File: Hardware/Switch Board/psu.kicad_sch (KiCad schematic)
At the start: 3 parts, among them J1 691218410003

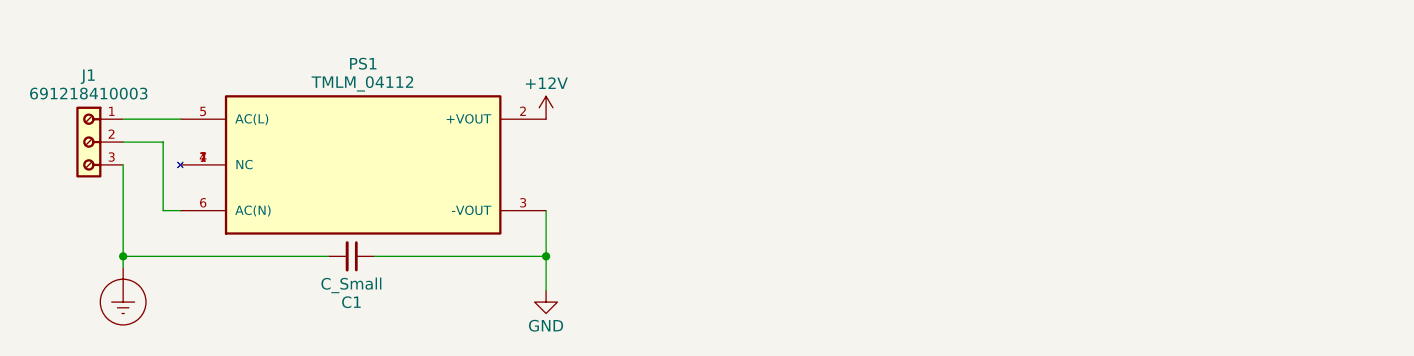
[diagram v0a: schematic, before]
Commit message: Completed Power Supply scheamatic + started to place components
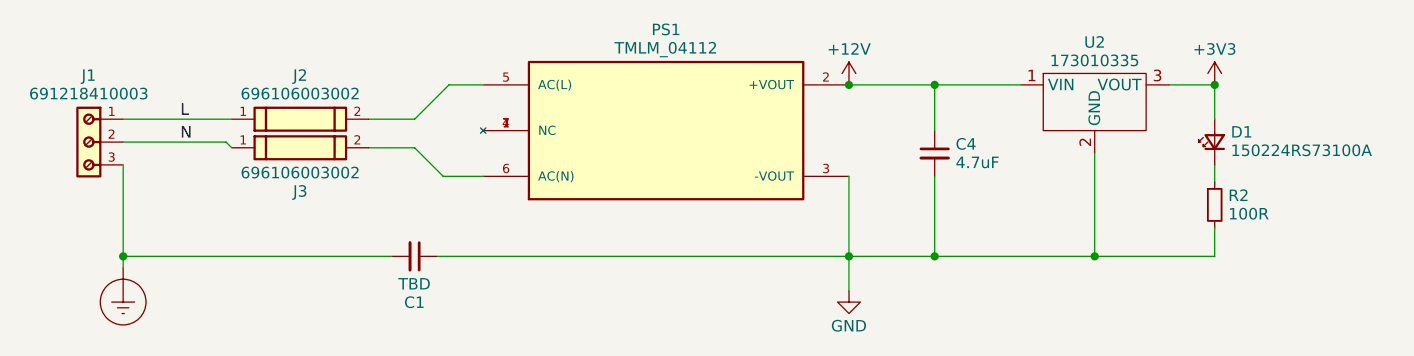
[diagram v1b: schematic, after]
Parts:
- added C4: 4.7uF, Capacitor_SMD:C_0805_2012Metric, symbol Device:C_Small
- added D1: 150224RS73100A, manul_tech:LED_2214, symbol manul_tech:150224RS73100A
- added J2, J3: 696106003002, manul_tech:696106003002, symbol manul_tech:696106003002
- added R2: 100R, Resistor_SMD:R_0805_2012Metric, symbol Device:R_Small
- added U2: 173010335, manul_tech:173010335, symbol manul_tech:173010335
- C1: value C_Small -> TBD; footprint (none) -> Capacitor_SMD:C_1206_3216Metric
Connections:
- net +12V: now also C4.1, U2.1 (VIN)
- net GND: now also C4.2, R2.2, U2.2 (GND)
- net at PS1.5 (AC(L)): now also J2.2; no longer J1.1
- net at PS1.6 (AC(N)): now also J3.2; no longer J1.2
- new net: D1.1 (K), R2.1
- new net +3V3: D1.2 (A), U2.3 (VOUT)
- new net L: J1.1, J2.1
- new net N: J1.2, J3.1
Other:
- moved on the sheet: C1, PS1
